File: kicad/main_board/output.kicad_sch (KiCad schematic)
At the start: 12 parts, among them J12 DRV1, J13 DRV2, J14 CH_IN, J15 CH1, J16 CH2, J17 CH3, J18 CH4

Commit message: connect charger VBUS before inrush limiter
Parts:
- renumbered R82 to R87
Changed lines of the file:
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@@
 	(title_block
 		(title "SW32 - Main Board")
-		(date "2024-05-29")
+		(date "2024-05-31")
 		(rev "1")
 		(company "saawsm")
@@
 		(dnp no)
 		(fields_autoplaced yes)
-		(property "Reference" "R82"
+		(property "Reference" "R87"
 			(at 95.25 62.2299 0)
 			(effects
@@
 			(project "main_board"
 				(path "/8e1f1504-76c2-49e6-9261-3c1190503f8c/1327ee6b-7a00-44f7-81fe-b42319e4569a"
-					(reference "R82")
+					(reference "R87")
 					(unit 1)
 				)

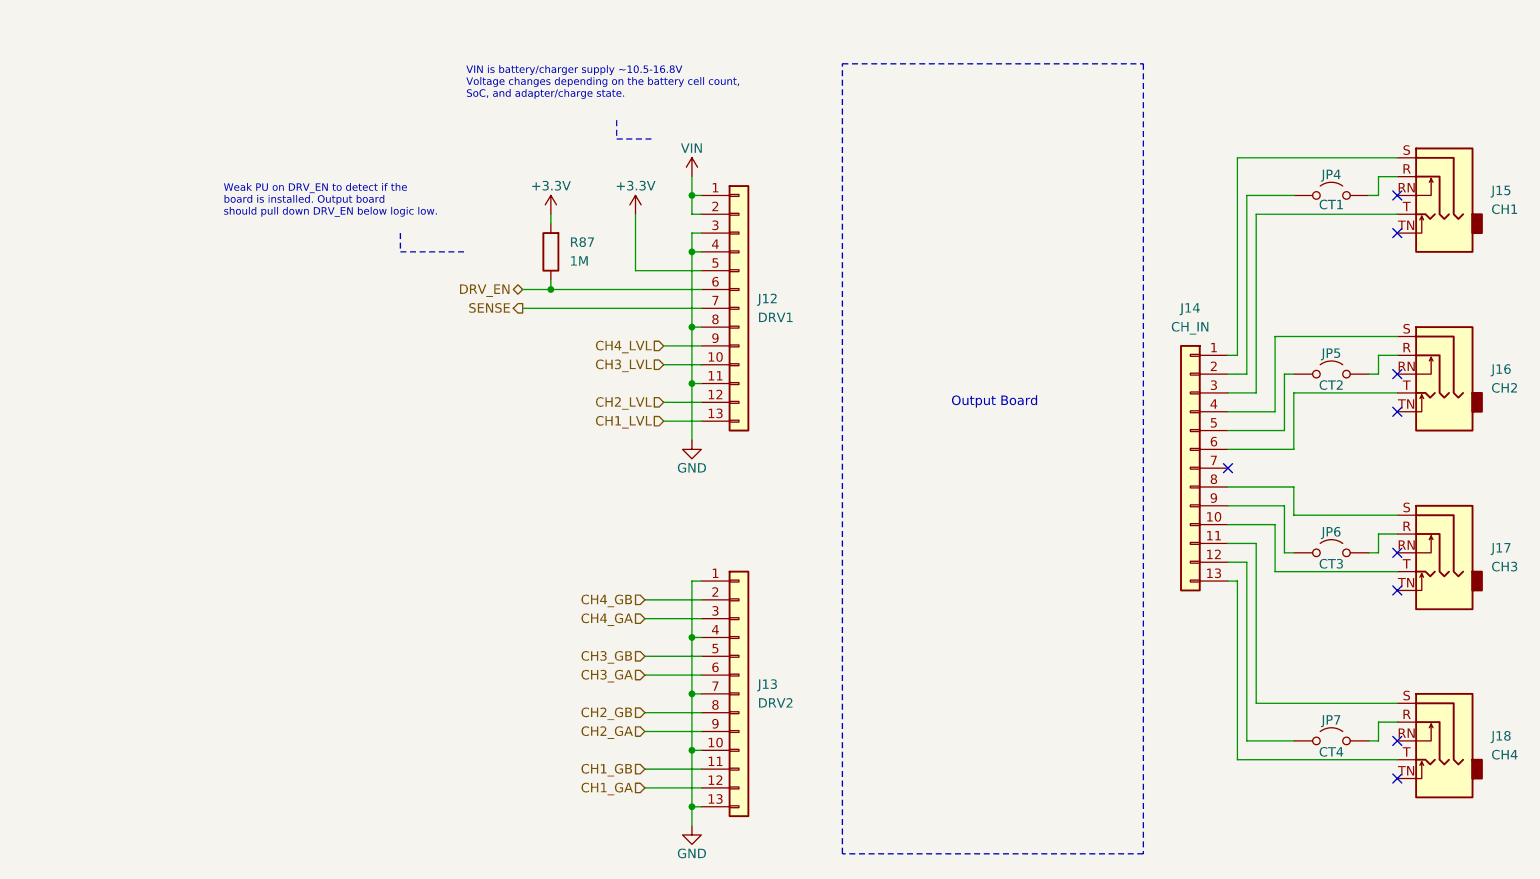
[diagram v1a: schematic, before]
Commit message: use 2x8 pin header
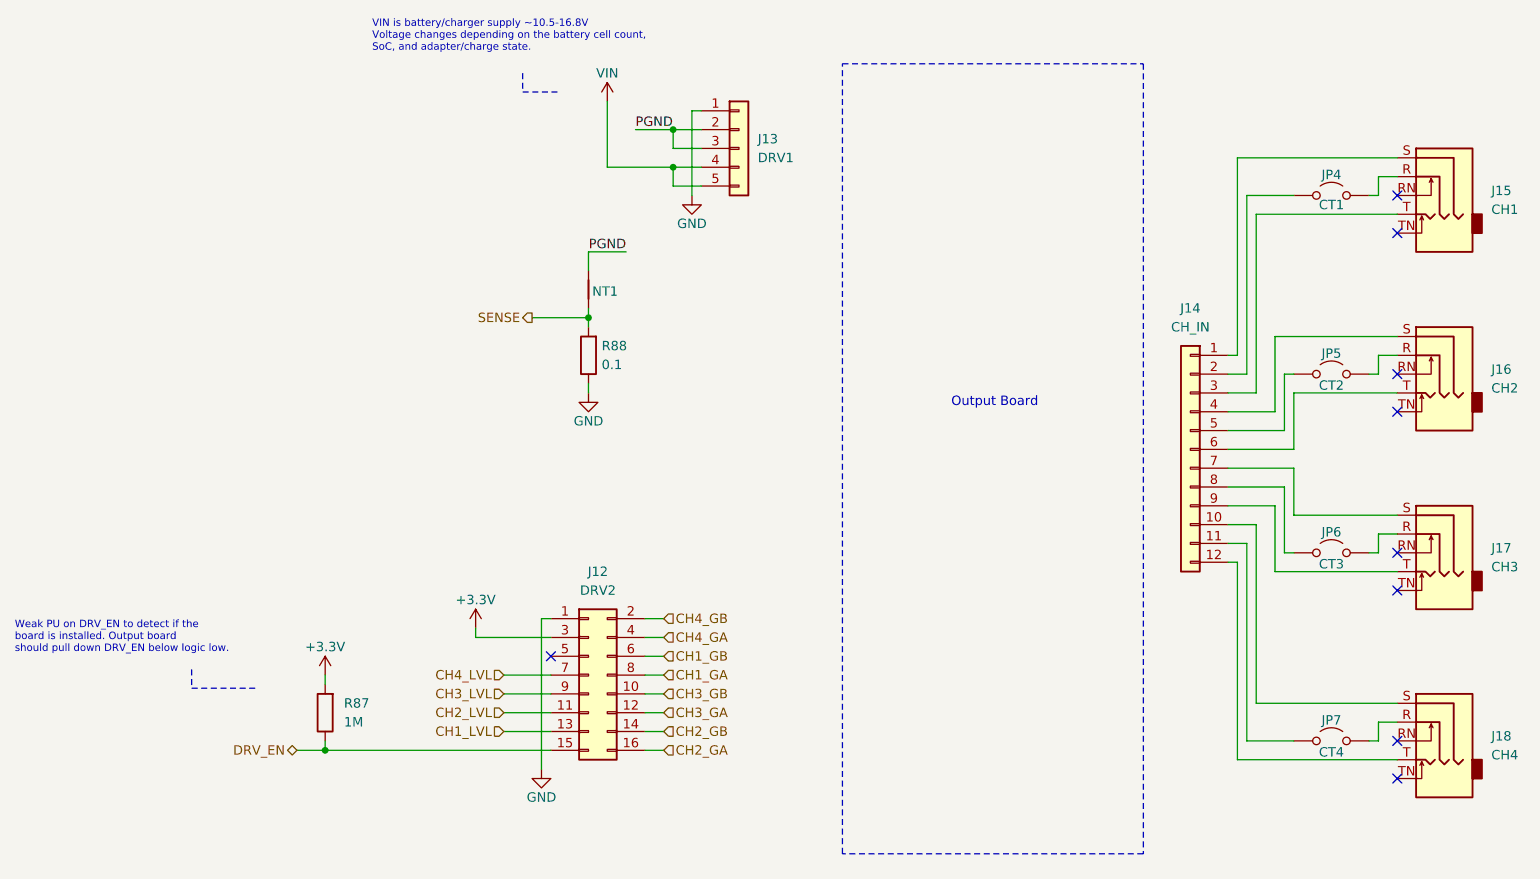
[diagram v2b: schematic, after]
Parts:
- added NT1: ~, NetTie:NetTie-2_SMD_Pad2.0mm, symbol Device:NetTie_2
- added R88: 0.1, Resistor_SMD:R_2512_6332Metric, symbol Device:R
- J12: renamed from J13; footprint Connector_PinSocket_2.54mm:PinSocket_1x13_P2.54mm_Vertical -> Connector_PinSocket_2.54mm:PinSocket_2x08_P2.54mm_Vertical; symbol Connector_Generic:Conn_01x13 -> Connector_Generic:Conn_02x08_Odd_Even; LCSC C2897376 -> C2897409
- J13: renamed from J12; footprint Connector_PinSocket_2.54mm:PinSocket_1x13_P2.54mm_Vertical -> Connector_PinSocket_2.54mm:PinSocket_1x05_P2.54mm_Vertical; symbol Connector_Generic:Conn_01x13 -> Connector_Generic:Conn_01x05; LCSC C2897376 -> C2897368
- J14: footprint Connector_PinSocket_2.54mm:PinSocket_1x13_P2.54mm_Vertical -> Connector_PinHeader_2.54mm:PinHeader_1x12_P2.54mm_Vertical; symbol Connector_Generic:Conn_01x13 -> Connector_Generic:Conn_01x12; LCSC C2897376 -> C2840012
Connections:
- net +3.3V: now also J12.3 (Pin_3); no longer J13.5 (Pin_5)
- net CH1_GA: now also J12.8 (Pin_8); no longer J12.12 (Pin_12)
- net CH1_GB: now also J12.6 (Pin_6); no longer J12.11 (Pin_11)
- net CH1_LVL: now also J12.13 (Pin_13); no longer J13.13 (Pin_13)
- net CH2_GA: now also J12.16 (Pin_16); no longer J12.9 (Pin_9)
- net CH2_GB: now also J12.14 (Pin_14); no longer J12.8 (Pin_8)
- net CH2_LVL: now also J12.11 (Pin_11); no longer J13.12 (Pin_12)
- net CH3_GA: now also J12.12 (Pin_12); no longer J12.6 (Pin_6)
- net CH3_GB: now also J12.10 (Pin_10); no longer J12.5 (Pin_5)
- net CH3_LVL: now also J12.9 (Pin_9); no longer J13.10 (Pin_10)
- net CH4_GA: now also J12.4 (Pin_4); no longer J12.3 (Pin_3)
- net CH4_LVL: now also J12.7 (Pin_7); no longer J13.9 (Pin_9)
- net DRV_EN: now also J12.15 (Pin_15); no longer J13.6 (Pin_6)
- net GND: now also J13.1 (Pin_1), R88.1; no longer J12.10 (Pin_10), J12.13 (Pin_13), J12.4 (Pin_4), J12.7 (Pin_7), J13.11 (Pin_11), J13.3 (Pin_3), J13.4 (Pin_4), J13.8 (Pin_8)
- net SENSE: now also NT1.1, R88.2; no longer J13.7 (Pin_7)
- net VIN: now also J13.4 (Pin_4), J13.5 (Pin_5); no longer J13.1 (Pin_1), J13.2 (Pin_2)
- net at JP6.1 (A): now also J14.8 (Pin_8); no longer J14.9 (Pin_9)
- net at JP7.1 (A): now also J14.11 (Pin_11); no longer J14.12 (Pin_12)
- net at J18.S: now also J14.10 (Pin_10); no longer J14.11 (Pin_11)
- net at J18.T: now also J14.12 (Pin_12); no longer J14.13 (Pin_13)
- net at J17.T: now also J14.9 (Pin_9); no longer J14.10 (Pin_10)
- net at J14.7 (Pin_7): now also J17.S
- new net PGND: J13.2 (Pin_2), J13.3 (Pin_3), NT1.2
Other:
- moved on the sheet: R87

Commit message: add draft output board
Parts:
- J12: value DRV2 -> DRV
- J13: value DRV1 -> DRV_PWR
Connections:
- net GND: now also J13.3 (Pin_3); no longer J13.1 (Pin_1)
- net PGND: now also J13.1 (Pin_1); no longer J13.3 (Pin_3)
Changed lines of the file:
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@@
 	)
 	(junction
-		(at 109.22 46.99)
+		(at 109.22 44.45)
 		(diameter 0)
 		(color 0 0 0 0)
@@
 	(wire
 		(pts
-			(xy 104.14 46.99) (xy 109.22 46.99)
+			(xy 104.14 44.45) (xy 109.22 44.45)
 		)
 		(stroke
@@
 	(wire
 		(pts
+			(xy 111.76 49.53) (xy 111.76 55.88)
+		)
+		(stroke
+			(width 0)
+			(type default)
+		)
+	)
+	(wire
+		(pts
 			(xy 190.5 85.09) (xy 184.15 85.09)
 		)
@@
 	(wire
 		(pts
-			(xy 109.22 46.99) (xy 109.22 49.53)
+			(xy 109.22 44.45) (xy 109.22 46.99)
 		)
 		(stroke
@@
 	(wire
 		(pts
-			(xy 111.76 44.45) (xy 111.76 55.88)
-		)
-		(stroke
-			(width 0)
-			(type default)
-		)
-	)
-	(wire
-		(pts
 			(xy 185.42 50.8) (xy 185.42 77.47)
 		)
@@
 	(wire
 		(pts
+			(xy 109.22 44.45) (xy 113.03 44.45)
+		)
+		(stroke
+			(width 0)
+			(type default)
+		)
+	)
+	(wire
+		(pts
 			(xy 109.22 46.99) (xy 113.03 46.99)
 		)
@@
 	(wire
 		(pts
-			(xy 109.22 49.53) (xy 113.03 49.53)
-		)
-		(stroke
-			(width 0)
-			(type default)
-		)
-	)
-	(wire
-		(pts
 			(xy 191.77 95.25) (xy 191.77 104.14)
 		)
@@
 	(wire
 		(pts
-			(xy 111.76 44.45) (xy 113.03 44.45)
+			(xy 111.76 49.53) (xy 113.03 49.53)
 		)
 		(stroke
@@
 	)
 	(label "PGND"
-		(at 104.14 46.99 0)
+		(at 104.14 44.45 0)
 		(fields_autoplaced yes)
 		(effects
@@
 			)
 		)
-		(property "Value" "DRV1"
+		(property "Value" "DRV_PWR"
 			(at 120.65 50.7999 0)
 			(effects
@@
 			)
 		)
-		(property "Value" "DRV2"
+		(property "Value" "DRV"
 			(at 99.06 109.22 0)
 			(effects

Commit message: add mainboard pcb
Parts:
- added NT2: ~, NetTie:NetTie-2_SMD_Pad2.0mm, symbol Device:NetTie_2
- renumbered R87 to R86, R88 to R87
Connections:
- net PGND: now also NT2.2
- net SENSE: now also NT2.1
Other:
- moved on the sheet: NT1, R87

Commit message: fix title block
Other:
- title: SW32 - Main Board -> SW32
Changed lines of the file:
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@@
 	(paper "A4")
 	(title_block
-		(title "SW32 - Main Board")
-		(date "2024-06-11")
+		(title "SW32")
+		(date "2024-06-12")
 		(rev "1")
 		(company "saawsm")
